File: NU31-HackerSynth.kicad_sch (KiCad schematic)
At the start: 109 parts, among them J1 Conn_02x07_Counter_Clockwise, J2 AudioJack3, J3 Barrel_Jack, Q1 NPN, Q2 NPN, Q3 NPN, SW1 SW_Push_DPDT, SW2 Run, U1 LM358, U2 LM358, U3 LM358, U4 4017, U5 LM358, U6 LM358, U7 LM358

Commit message: Updated schematics layout, added clock input and output jacks and CV output jack, changed sequence length jumper pins from 7x2 to 8x2 (2 pins unconnected, just to keep the jumper)
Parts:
- removed RV4, RV5 (x2): 100kB, Rumblesan_Footprints:Potentiometer_Alpha_RD901F-40-00D_Single_Vertical_CircularHoles, symbol Device:R_Potentiometer
- added C14, C15, C16, C17, C18: 100n, symbol Device:C
- added J4, J5, J6: AudioJack2_SwitchT, symbol Connector_Audio:AudioJack2_SwitchT
- added JP1, JP2, JP3, JP4, JP5, JP6, JP7: Jumper_2_Bridged, symbol Jumper:Jumper_2_Bridged
- added R52, R54, R56, R9: R51k, symbol Device:R
- added R53, R55, R8: 3k3, Rumblesan_Footprints:R_Axial_DIN0207_L6.3mm_D2.5mm_P7.62mm_Horizontal, symbol Device:R
- added RV13, RV14, RV5: 100kB, Rumblesan_Footprints:Potentiometer_Alpha_RD901F-40-00D_Single_Vertical_CircularHoles, symbol Device:R_Potentiometer
- added unit 1 of U6
- added unit 3 of U7
- J1: symbol Connector_Generic:Conn_02x07_Counter_Clockwise -> Connector_Generic:Conn_02x08_Counter_Clockwise
- R25, R27, R29: value 3k3 -> R51k; footprint Rumblesan_Footprints:R_Axial_DIN0207_L6.3mm_D2.5mm_P7.62mm_Horizontal -> (none)
- R7: value 50k -> 51k
- SW2: value Run -> SW_SPDT; footprint Rumblesan_Footprints:SW_SPDT_DailyWell_MiniToggle -> (none)
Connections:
- net VCA CV In is gone; now on an unnamed net: R11.1
- net +VDC: now also C2.1, U2.8 (V+), U3.8 (V+), U5.8 (V+), U6.4 (V-), C14.1, C15.1, C16.1, C17.1, C18.1, U7.4 (V-)
- net CLOCK_OUT: now also J5.T, J6.T, JP5.1 (A), JP6.1 (A); no longer R44.1
- net GND: now also C2.2, R25.2, R27.2, R29.2, U2.4 (V-), U3.4 (V-), U5.4 (V-), U6.8 (V+), C14.2, C15.2, C16.2, C17.2, C18.2, J4.S, J5.S, J6.S, R52.2, R54.2, R56.2, R9.2, RV13.3, RV14.3, RV5.3, U7.8 (V+)
- net at R26.1, U4.7 (Q3): now also J1.14 (Pin_14), RV7.1; no longer J1.12 (Pin_12)
- net at R45.2, R46.2, U6.5 (+): now also U6.2 (-); no longer U6.2 (-)
- net at D17.2 (A): now also R55.2; no longer R30.2
- net at R30.1, RV9.1: now also J1.12 (Pin_12), U4.1 (Q5); no longer J1.8 (Pin_8), U4.6 (Q7)
- net at R41.2, R44.2, RV11.1: now also U6.1; no longer U6.1
- net at Q2.2 (B), R10.2: no longer R11.2
- net SEQ_CV_OUT: now reaches D10.1 (K), D12.1 (K), D14.1 (K), D16.1 (K), D18.1 (K), D4.1 (K), D6.1 (K), D8.1 (K)
- net SEQ_CV_OUT: now also J4.T, JP1.1 (A), JP2.1 (A)
- net at RV9.2: now also D14.2 (A), R52.1; no longer D18.2 (A)
- net at R41.1, R43.1: now also U6.3 (+); no longer U6.3 (+)
- net at D13.2 (A): now also R30.2; no longer R28.2
- net at D7.2 (A): now also R24.2; no longer R25.2
- net at D11.2 (A): now also R28.2; no longer R27.2
- net at D6.2 (A): now also R9.1, RV5.2
- net at D8.2 (A): now also R25.1, RV6.2
- net at D10.2 (A): now also R27.1, RV7.2
- net at D12.2 (A): now also R29.1, RV8.2; no longer RV6.2
- net at D15.2 (A): now also R53.2; no longer R29.2
- net at D5.2 (A): now also R8.2; no longer R24.2
- net at D16.2 (A): now also R54.1, RV13.2; no longer RV8.2
- net SEQ_CLOCK_IN: now reaches SW2.1 (A)
- net SEQ_CLOCK_IN: now also JP6.2 (B)
- net Amp_In renamed AMP_IN
- net AMP_IN: now also JP7.2 (B)
- net CLOCK: no longer names the net of SW2.3 (C)
- net Decay_In renamed DECAY_TRIG_IN
- net DECAY_TRIG_IN: now also JP5.2 (B)
- net Decay_Out renamed DECAY_CV_OUT
- net DECAY_CV_OUT: now also JP4.1 (A)
- net Mix_Out renamed MIX_OUT
- net MIX_OUT: now also JP3.1 (A)
- net Pitch CV In renamed OSC1_CV_IN
- net OSC1_CV_IN: now also JP1.2 (B); no longer R16.1, RV3.1
- net Square 1 renamed SQ1_OUT
- net Square 2 renamed SQ2_OUT
- net Triangle 1 renamed TRI1_OUT
- net Triangle 2 renamed TRI2_OUT
- net VCA In renamed VCA_SIGNAL_IN
- net VCA_SIGNAL_IN: now also JP3.2 (B)
- net VCA Out renamed VCA_OUT
- net VCA_OUT: now also JP7.1 (A)
- new net: J1.13 (Pin_13), R28.1, RV8.1, U4.10 (Q4)
- new net: J1.16 (Pin_16), R8.1, RV5.1, U4.2 (Q1)
- new net: J1.15 (Pin_15), R24.1, RV6.1, U4.4 (Q2)
- new net: J1.11 (Pin_11), R53.1, RV13.1, U4.5 (Q6)
- new net: J1.10 (Pin_10), R55.1, RV14.1, U4.6 (Q7)
- new net: D18.2 (A), R56.1, RV14.2
- new net: J5.TN, R44.1
- new net OSC2_CV_IN: JP2.2 (B), R16.1, RV3.1
- new net VCA_CV_IN: JP4.2 (B), R11.2
- now unconnected: J1.9 (Pin_9)
- no-connect marks 3 -> 7
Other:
- note added: "CV Out"
- note added: "Detune"
- note added: "External Clock Input"
- note added: "External Clock Output"
- note added: "Fine-tune"
- note added: "Oscillator 2 (with detune)"
- note added: "Routing"
- note added: "Sequence Length Jumper"
- note added: "VCA"
- note removed: "Oscillator 2"
- note removed: "VCA/LPG"
- note removed: "Схема від Кості https://tinyurl.com/yusjdvon"
- company: (none) -> NU31 Hackerspace
- title: (none) -> Space Cow
- moved on the sheet: C1, C10, C11, C12, C13, C2, C3, C4, C5, C6, C7, C8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

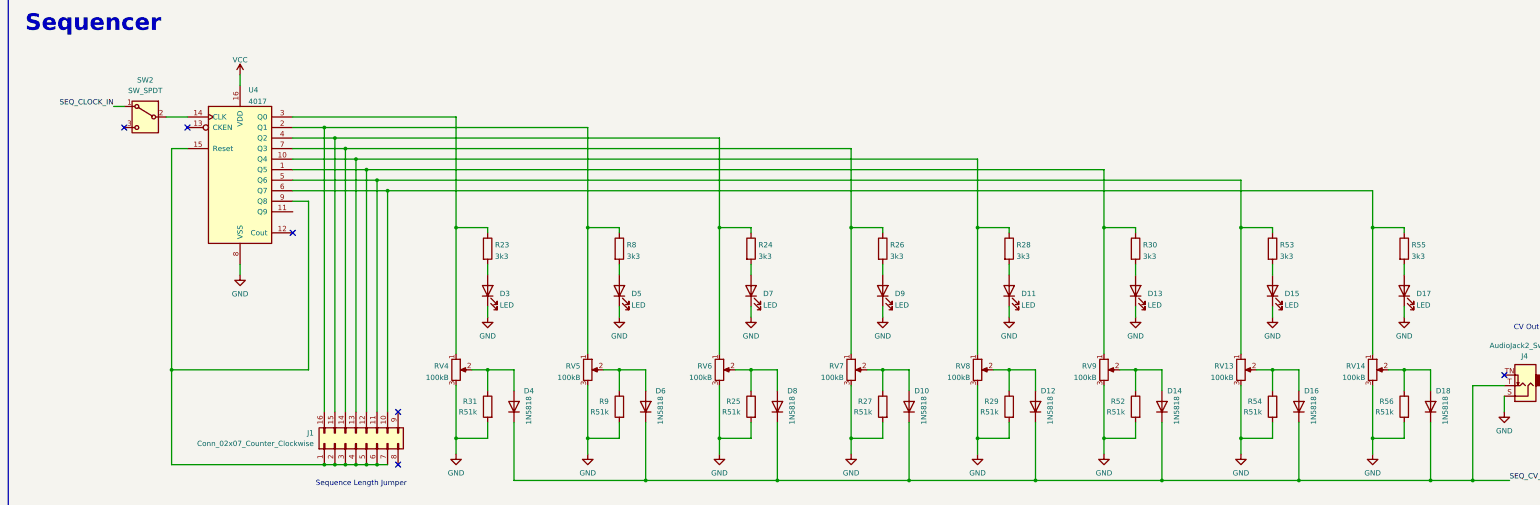
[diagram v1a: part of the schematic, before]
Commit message: Grounded CKEN and CLK switch, switched diodes in sequencer to 1N4148
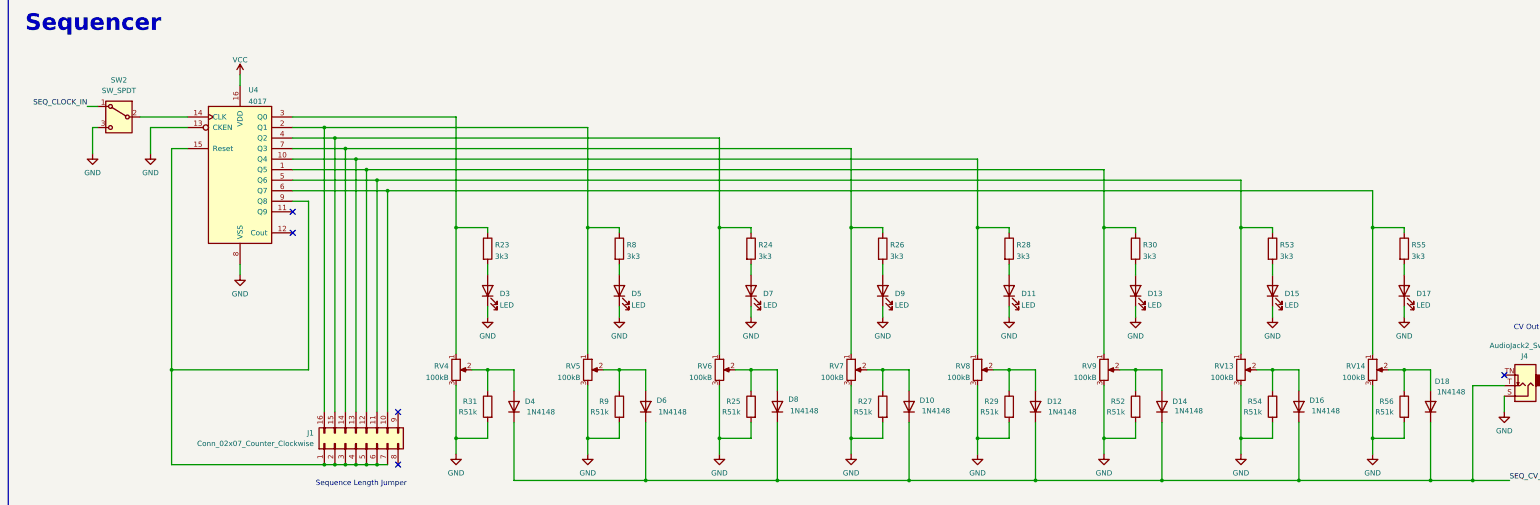
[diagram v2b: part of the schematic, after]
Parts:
- D10, D12, D14, D16, D18, D4, D6, D8: value 1N5818 -> 1N4148
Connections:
- net GND: now also SW2.3 (C), U4.13 (CKEN)
- no-connect marks 7 -> 6
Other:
- moved on the sheet: SW2
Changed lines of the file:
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@@
 	)
 	(no_connect
-		(at 109.22 441.96)
+		(at 83.82 381)
 	)
 	(no_connect
-		(at 43.18 360.68)
+		(at 109.22 441.96)
 	)
 	(no_connect
 		(at 83.82 386.08)
 	)
-	(no_connect
-		(at 58.42 360.68)
+	(wire
+		(pts
+			(xy 49.53 360.68) (xy 58.42 360.68)
+		)
+		(stroke
+			(width 0)
+			(type default)
+		)
 	)
 	(wire
@@
 	(wire
 		(pts
+			(xy 49.53 367.03) (xy 49.53 360.68)
+		)
+		(stroke
+			(width 0)
+			(type default)
+		)
+	)
+	(wire
+		(pts
 			(xy 74.93 492.76) (xy 74.93 502.92)
 		)
@@
 	(wire
 		(pts
+			(xy 35.56 367.03) (xy 35.56 360.68)
+		)
+		(stroke
+			(width 0)
+			(type default)
+		)
+	)
+	(wire
+		(pts
 			(xy 186.69 435.61) (xy 186.69 439.42)
 		)
@@
 	(wire
 		(pts
-			(xy 53.34 358.14) (xy 58.42 358.14)
+			(xy 46.99 358.14) (xy 58.42 358.14)
 		)
 		(stroke
@@
 	(wire
 		(pts
+			(xy 35.56 360.68) (xy 36.83 360.68)
+		)
+		(stroke
+			(width 0)
+			(type default)
+		)
+	)
+	(wire
+		(pts
 			(xy 130.81 262.89) (xy 130.81 265.43)
 		)
@@
 	(wire
 		(pts
-			(xy 40.64 355.6) (xy 43.18 355.6)
+			(xy 34.29 355.6) (xy 36.83 355.6)
 		)
 		(stroke
@@
 	)
 	(label "SEQ_CLOCK_IN"
-		(at 40.64 355.6 180)
+		(at 34.29 355.6 180)
 		(effects
 			(font
@@
 		(dnp no)
 		(property "Reference" "D6"
-			(at 173.736 424.18 90)
+			(at 173.99 426.466 90)
 			(effects
 				(font
@@
 			)
 		)
-		(property "Value" "1N5818"
-			(at 172.466 425.45 0)
+		(property "Value" "1N4148"
+			(at 178.816 429.26 90)
 			(effects
 				(font
@@
 		(dnp no)
 		(property "Reference" "D12"
-			(at 267.716 424.18 90)
+			(at 269.24 426.72 90)
 			(effects
 				(font
@@
 			)
 		)
-		(property "Value" "1N5818"
-			(at 266.446 425.45 0)
+		(property "Value" "1N4148"
+			(at 272.796 429.26 90)
 			(effects
 				(font
@@
 		(dnp no)
 		(property "Reference" "D4"
-			(at 141.986 424.18 90)
+			(at 142.24 426.72 90)
 			(effects
 				(font
@@
 			)
 		)
-		(property "Value" "1N5818"
-			(at 140.716 425.45 0)
+		(property "Value" "1N4148"
+			(at 147.066 429.26 90)
 			(effects
 				(font
@@
 	)
 	(symbol
+		(lib_id "power:GND")
+		(at 35.56 367.03 0)
+		(unit 1)
+		(exclude_from_sim no)
+		(in_bom yes)
+		(on_board yes)
+		(dnp no)
+		(fields_autoplaced yes)
+		(property "Reference" "#PWR056"
+			(at 35.56 373.38 0)
+			(effects
+				(font
+					(size 1.27 1.27)
+				)
+				(hide yes)
+			)
+		)
+		(property "Value" "GND"
+			(at 35.56 371.5925 0)
+			(effects
+				(font
+					(size 1.27 1.27)
+				)
+			)
+		)
+		(property "Footprint" ""
+			(at 35.56 367.03 0)
+			(effects
+				(font
+					(size 1.27 1.27)
+				)
+				(hide yes)
+			)
+		)
+		(property "Datasheet" ""
+			(at 35.56 367.03 0)
+			(effects
+				(font
+					(size 1.27 1.27)
+				)
+				(hide yes)
+			)
+		)
+		(property "Description" ""
+			(at 35.56 367.03 0)
+			(effects
+				(font
+					(size 1.27 1.27)
+				)
+			)
+		)
+		(pin "1"
+		)
+		(instances
+			(project "NU31-HackerSynth"
+				(path "/151a4108-ccd8-4864-9fa1-a2e140a3decb"
+					(reference "#PWR056")
+					(unit 1)
+				)
+			)
+		)
+	)
+	(symbol
 		(lib_id "Device:R_Potentiometer")
 		(at 279.4 419.1 0)
@@
 	)
 	(symbol
+		(lib_id "power:GND")
+		(at 49.53 367.03 0)
+		(unit 1)
+		(exclude_from_sim no)
+		(in_bom yes)
+		(on_board yes)
+		(dnp no)
+		(fields_autoplaced yes)
+		(property "Reference" "#PWR055"
+			(at 49.53 373.38 0)
+			(effects
+				(font
+					(size 1.27 1.27)
+				)
+				(hide yes)
+			)
+		)
+		(property "Value" "GND"
+			(at 49.53 371.5925 0)
+			(effects
+				(font
+					(size 1.27 1.27)
+				)
+			)
+		)
+		(property "Footprint" ""
+			(at 49.53 367.03 0)
+			(effects
+				(font
+					(size 1.27 1.27)
+				)
+				(hide yes)
+			)
+		)
+		(property "Datasheet" ""
+			(at 49.53 367.03 0)
+			(effects
+				(font
+					(size 1.27 1.27)
+				)
+				(hide yes)
+			)
+		)
+		(property "Description" ""
+			(at 49.53 367.03 0)
+			(effects
+				(font
+					(size 1.27 1.27)
+				)
+			)
+		)
+		(pin "1"
+		)
+		(instances
+			(project "NU31-HackerSynth"
+				(path "/151a4108-ccd8-4864-9fa1-a2e140a3decb"
+					(reference "#PWR055")
+					(unit 1)
+				)
+			)
+		)
+	)
+	(symbol
 		(lib_id "power:+VDC")
 		(at 36.83 546.1 0)
@@
 		(lib_name "SW_SPDT_1")
 		(lib_id "Switch:SW_SPDT")
-		(at 48.26 358.14 0)
+		(at 41.91 358.14 0)
 		(mirror y)
 		(unit 1)
@@
 		(fields_autoplaced yes)
 		(property "Reference" "SW2"
-			(at 48.26 349.25 0)
+			(at 41.91 349.25 0)
 			(effects
 				(font
@@
 		)
 		(property "Value" "SW_SPDT"
-			(at 48.26 351.79 0)
+			(at 41.91 351.79 0)
 			(effects
 				(font
@@
 		)
 		(property "Footprint" ""
-			(at 48.26 358.14 0)
+			(at 41.91 358.14 0)
 			(effects
 				(font
@@
 		)
 		(property "Datasheet" "~"
-			(at 48.26 365.76 0)
+			(at 41.91 365.76 0)
 			(effects
 				(font
@@
 		)
 		(property "Description" "Switch, single pole double throw"
-			(at 48.26 358.14 0)
+			(at 41.91 358.14 0)
 			(effects
 				(font
@@
 		(dnp no)
 		(property "Reference" "D8"
-			(at 205.486 424.18 90)
+			(at 205.74 426.212 90)
 			(effects
 				(font
@@
 			)
 		)
-		(property "Value" "1N5818"
-			(at 204.216 425.45 0)
+		(property "Value" "1N4148"
+			(at 210.566 429.006 90)
 			(effects
 				(font
@@
 		(dnp no)
 		(property "Reference" "D14"
-			(at 298.196 424.18 90)
+			(at 299.466 426.72 90)
 			(effects
 				(font
@@
 			)
 		)
-		(property "Value" "1N5818"
-			(at 296.926 425.45 0)
+		(property "Value" "1N4148"
+			(at 303.276 429.006 90)
 			(effects
 				(font
@@
 		(dnp no)
 		(property "Reference" "D10"
-			(at 237.236 424.18 90)
+			(at 238.506 426.466 90)
 			(effects
 				(font
@@
 			)
 		)
-		(property "Value" "1N5818"
-			(at 235.966 425.45 0)
+		(property "Value" "1N4148"
+			(at 242.316 429.006 90)
 			(effects
 				(font
@@
 		(dnp no)
 		(property "Reference" "D18"
-			(at 362.966 424.18 90)
+			(at 362.712 421.894 90)
 			(effects
 				(font
@@
 			)
 		)
-		(property "Value" "1N5818"
-			(at 361.696 425.45 0)
+		(property "Value" "1N4148"
+			(at 366.522 424.434 90)
 			(effects
 				(font
@@
 		(dnp no)
 		(property "Reference" "D16"
-			(at 331.216 424.18 90)
+			(at 332.486 426.466 90)
 			(effects
 				(font
@@
 			)
 		)
-		(property "Value" "1N5818"
-			(at 329.946 425.45 0)
+		(property "Value" "1N4148"
+			(at 336.296 429.006 90)
 			(effects
 				(font

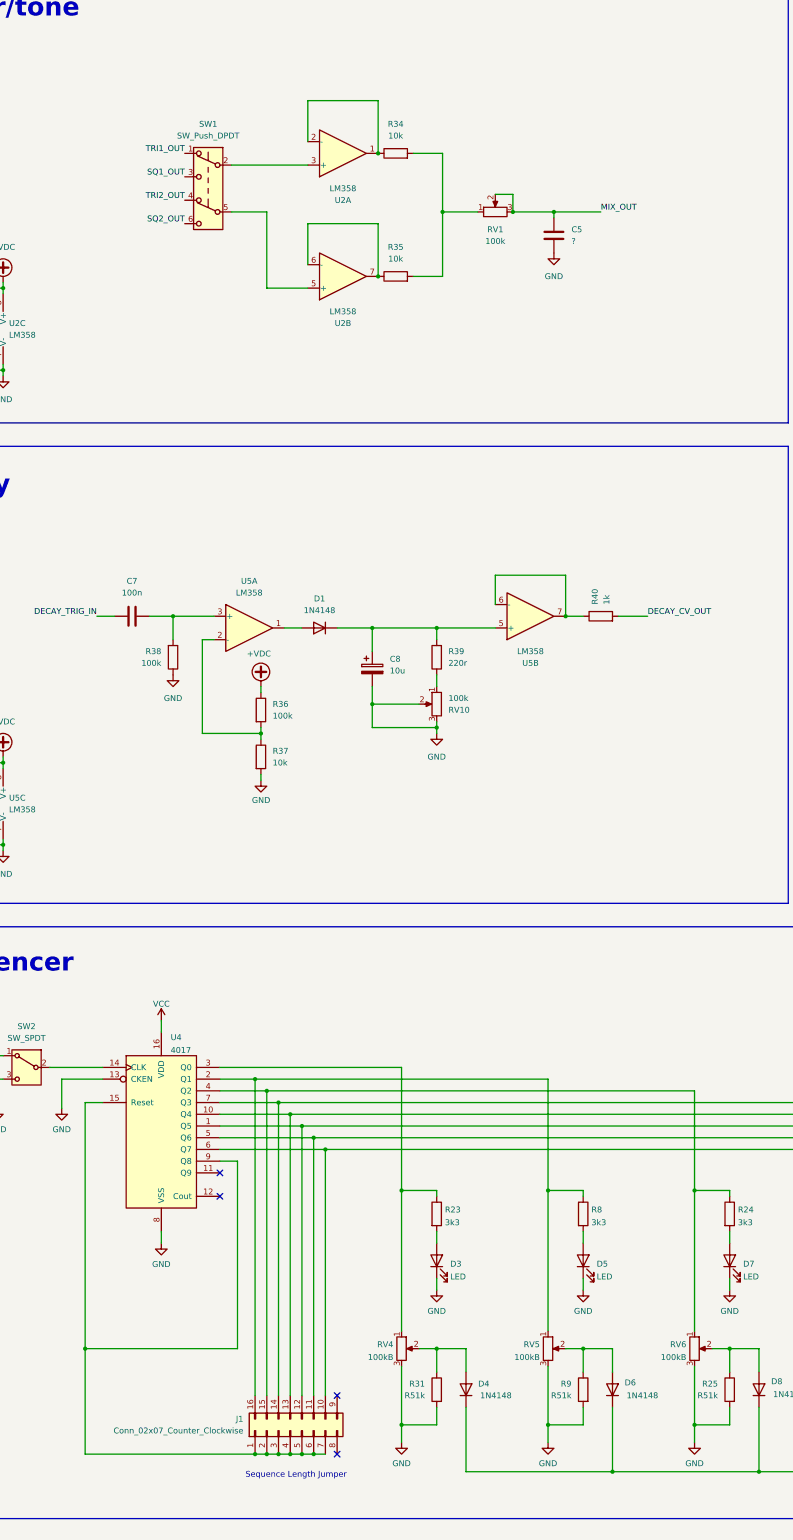
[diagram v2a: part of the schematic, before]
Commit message: Added buffer to mixer output, connected last step reset jumper pins
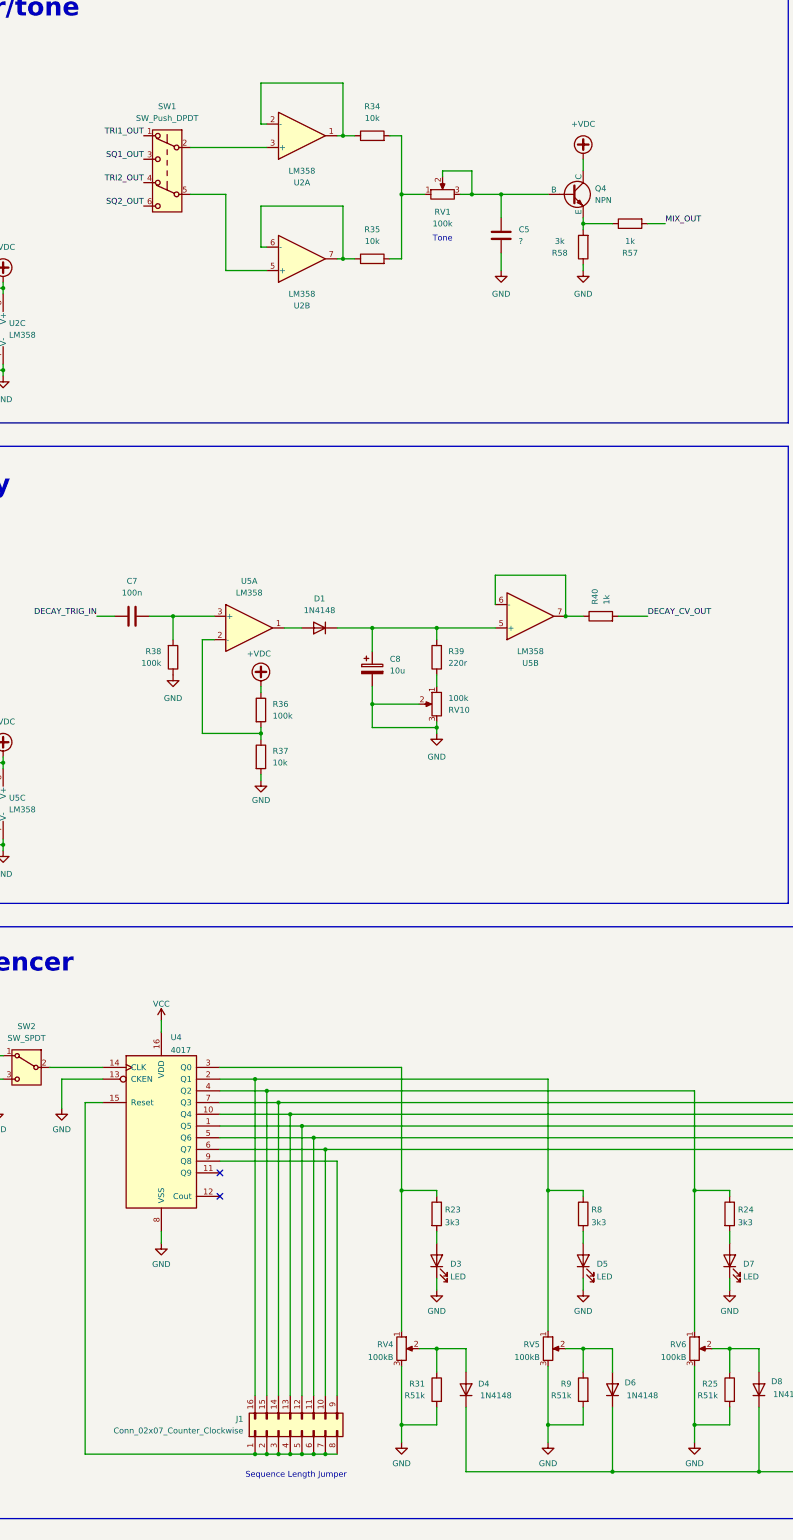
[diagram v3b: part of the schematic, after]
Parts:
- added Q4: NPN, symbol Simulation_SPICE:NPN
- added R57: 1k, symbol Device:R
- added R58: 3k, symbol Device:R
- D1: footprint Diode_THT:D_DO-35_SOD27_P7.62mm_Horizontal -> (none)
- D10, D12, D14, D16, D18, D4, D6, D8: footprint Rumblesan_Footprints:D_DO-35_SOD27_P7.62mm_Horizontal -> (none)
- D11, D13, D15, D17, D3, D5, D7, D9: footprint LED_THT:LED_D5.0mm -> (none)
- R23, R24, R26, R28, R30, R53, R55, R8: footprint Rumblesan_Footprints:R_Axial_DIN0207_L6.3mm_D2.5mm_P7.62mm_Horizontal -> (none)
- RV13, RV14, RV4, RV5, RV6, RV7, RV8, RV9: footprint Rumblesan_Footprints:Potentiometer_Alpha_RD901F-40-00D_Single_Vertical_CircularHoles -> (none)
- U4: footprint Package_DIP:DIP-16_W7.62mm -> (none)
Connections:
- net +VDC: now also Q4.1 (C)
- net GND: now also R58.1
- net MIX_OUT: now also R57.2; no longer C5.1, RV1.2, RV1.3
- net at J1.1 (Pin_1), J1.2 (Pin_2), J1.3 (Pin_3)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: now also J1.8 (Pin_8); no longer U4.9 (Q8)
- net at J1.9 (Pin_9): now also U4.9 (Q8)
- new net: C5.1, Q4.2 (B), RV1.2, RV1.3
- new net: Q4.3 (E), R57.1, R58.2
- no-connect marks 6 -> 4
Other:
- note added: "Tone"
- moved on the sheet: C5, R34, R35, RV1, SW1, U2A, U2B
